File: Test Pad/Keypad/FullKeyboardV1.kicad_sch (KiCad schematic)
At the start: 57 parts, among them SW5 double_key

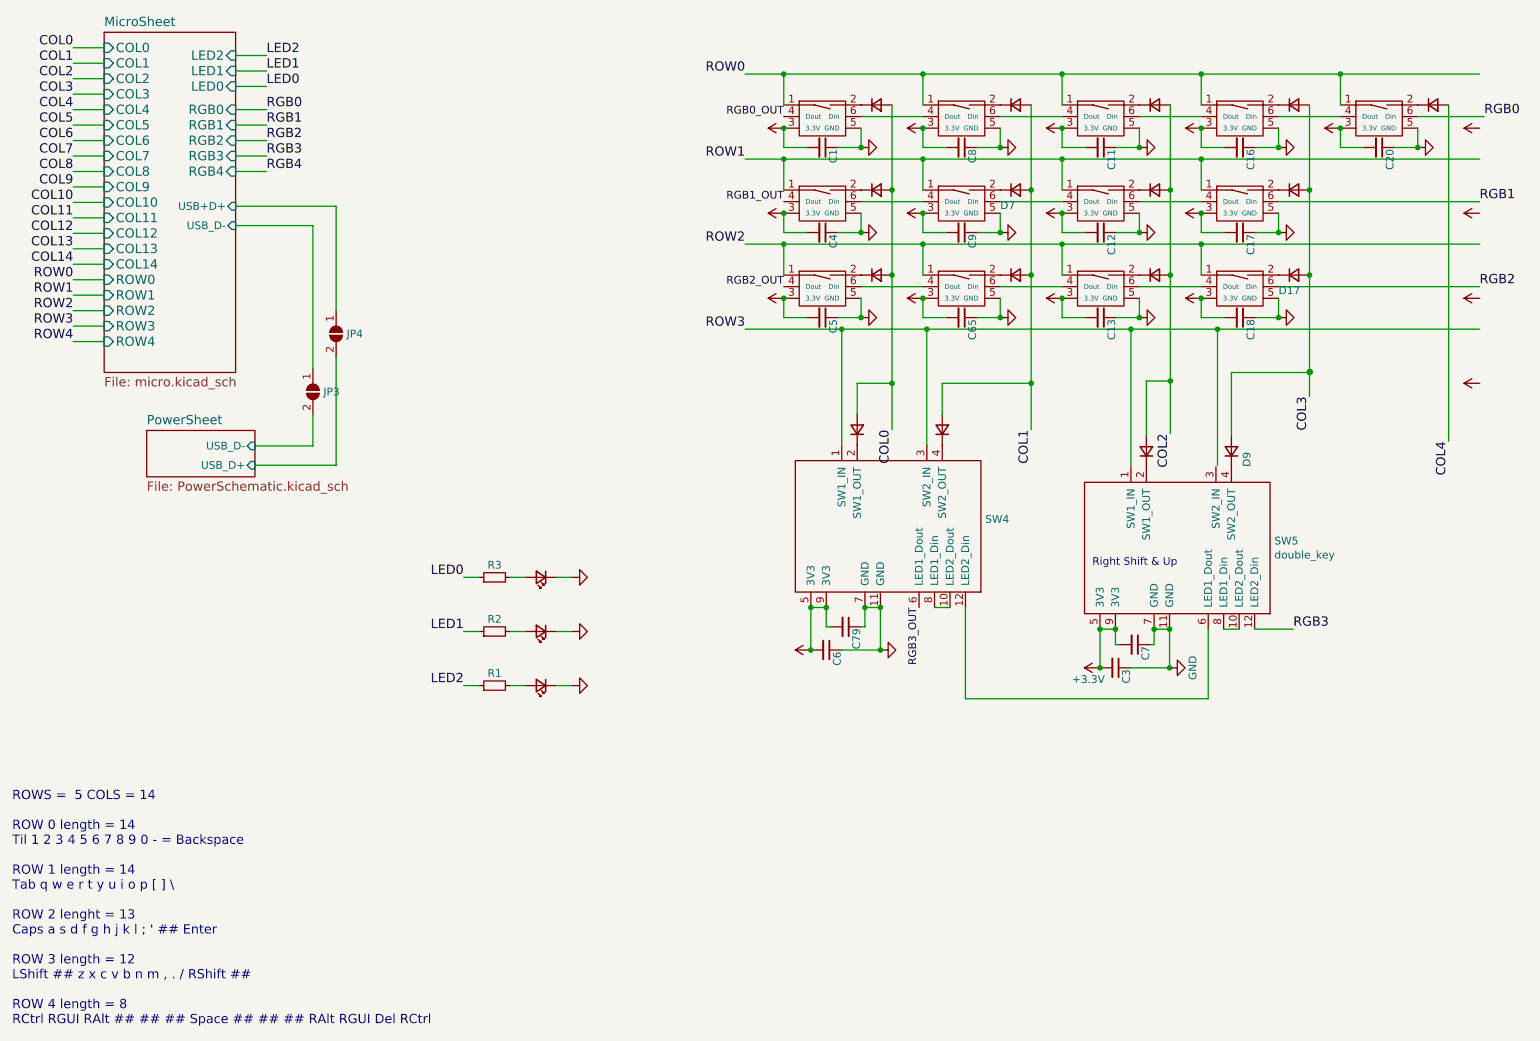
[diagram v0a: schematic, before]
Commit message: Started nucleo 144 test pad and keypad boards
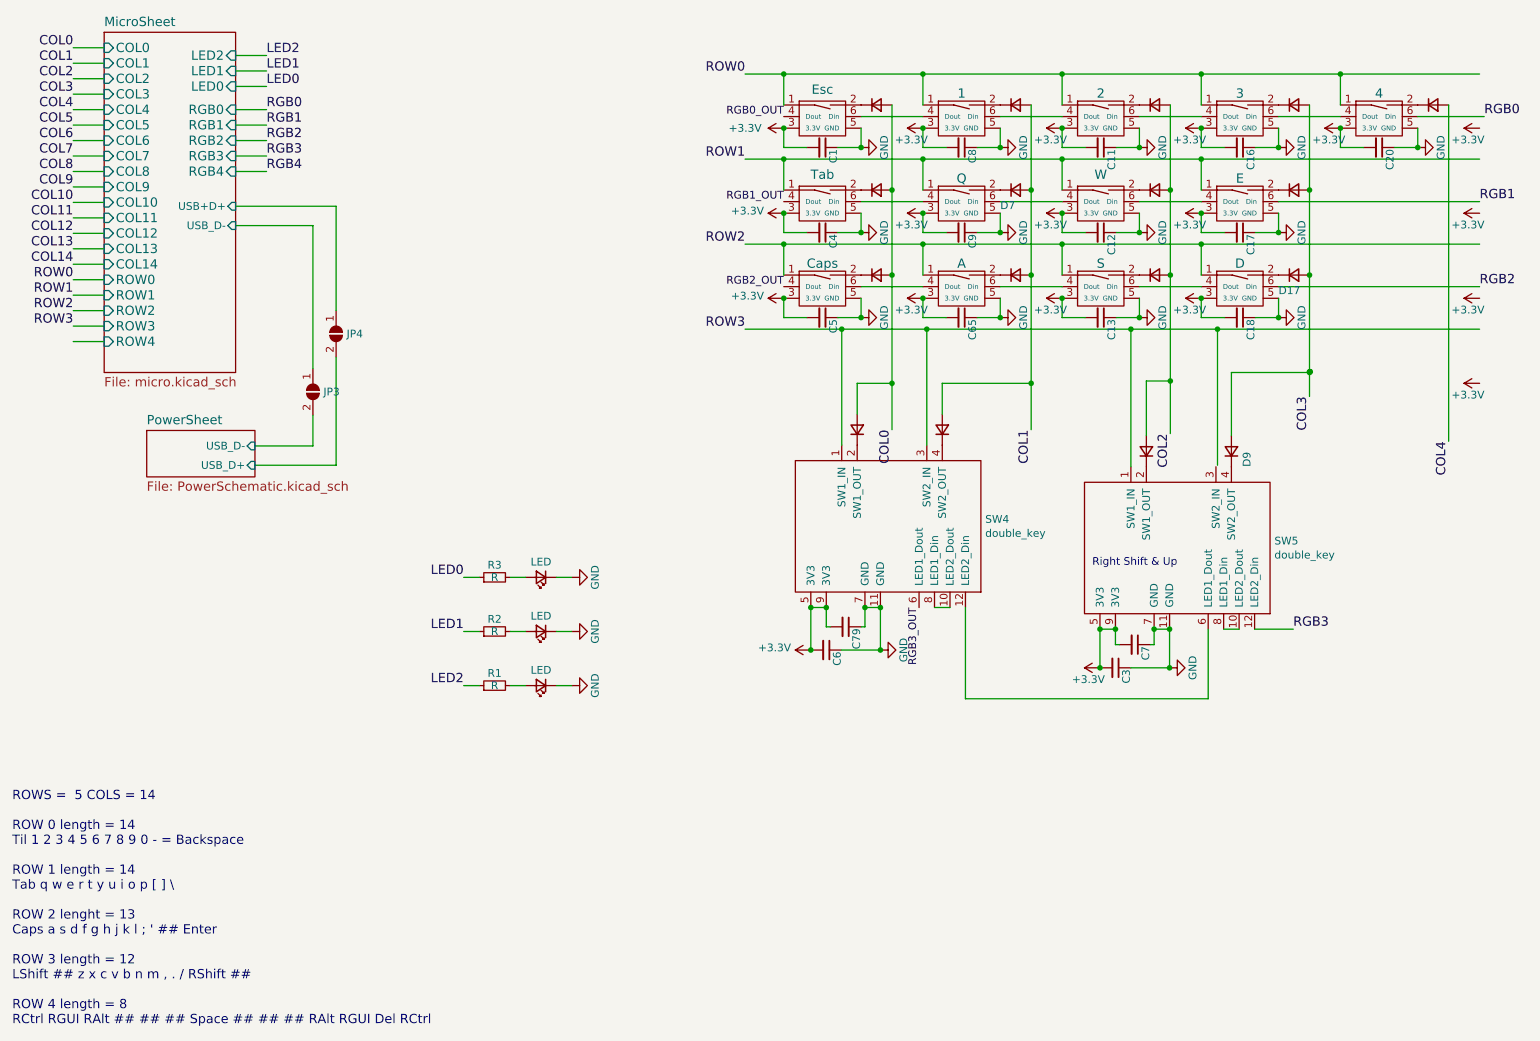
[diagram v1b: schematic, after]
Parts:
- C1, C11, C12, C13, C16, C17, C18, C20, C4, C5, C6, C65, C79, C8, C9: value (none) -> C_Small; footprint (none) -> Capacitor_SMD:C_0603_1608Metric
- D1, D10, D11, D12, D15, D16, D17, D19, D2, D3, D4, D6, D7, D77, D8: value (none) -> D_Small; footprint (none) -> Diode_SMD:D_SOD-123
- D70, D71, D72: value (none) -> LED; footprint (none) -> LED_SMD:LED_0603_1608Metric
- JP3, JP4: value (none) -> SolderJumper_2_Open; footprint (none) -> Jumper:SolderJumper-2_P1.3mm_Open_RoundedPad1.0x1.5mm
- R1, R2, R3: value (none) -> R; footprint (none) -> Resistor_SMD:R_0603_1608Metric
- SW1: value (none) -> Esc
- SW10: value (none) -> 2
- SW11: value (none) -> W
- SW12: value (none) -> S
- SW15: value (none) -> 3
- SW16: value (none) -> E
- SW17: value (none) -> D
- SW19: value (none) -> 4
- SW2: value (none) -> Tab
- SW3: value (none) -> Caps
- SW4: value (none) -> double_key; footprint (none) -> keyboard:RGB_CHERRY_SHIFT_ROW_LEFT
- SW6: value (none) -> 1
- SW7: value (none) -> Q
- SW8: value (none) -> A
